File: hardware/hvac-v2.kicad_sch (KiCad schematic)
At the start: 143 parts

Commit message: Start hardware revision 2.3: fix LCD I2C
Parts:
- BZ1: value (none) -> Buzzer; footprint (none) -> Homebrew:MURATA_PKM13EPYH4000-A0
- C1, C14, C38, C9: value (none) -> 4.7uF; footprint (none) -> Capacitor_SMD:C_0603_1608Metric
- C10, C11, C15, C16: value (none) -> 0.22uF; footprint (none) -> Capacitor_SMD:C_0805_2012Metric
- C12, C13, C17, C18, C2, C21, C22, C23, C24, C25, C26, C27, C28, C29, C30, C31, C32, C33, C34, C35, C36, C37, C4, C40, C41, C42, C43, C5, C6, C7, C8: value (none) -> 0.1uF; footprint (none) -> Capacitor_SMD:C_0402_1005Metric
- C19, C39: value (none) -> 1000uF; footprint (none) -> Capacitor_THT:CP_Radial_D10.0mm_P5.00mm
- C20, C3: value (none) -> 1nF; footprint (none) -> Capacitor_SMD:C_0402_1005Metric
- D1, D10, D11, D12, D13, D14, D15, D19, D2, D20, D21, D22, D23, D24, D6, D7: value (none) -> TVS_5V; footprint (none) -> Diode_SMD:D_SOD-323
- D16, D17, D18, D3, D8, D9: value (none) -> D_Schottky; footprint (none) -> Diode_THT:D_DO-201AD_P12.70mm_Horizontal
- D4: value (none) -> TVS_12V; footprint (none) -> Diode_SMD:D_SMB_Handsoldering
- D5: value (none) -> LED; footprint (none) -> LED_SMD:LED_0805_2012Metric
- F1: value (none) -> ATC; footprint (none) -> Homebrew:FUSE_3550-2
- H1, H2, H3, H4, H5: value (none) -> HOLE; footprint (none) -> Homebrew:HOLE_M4
- H6: value (none) -> SLOT; footprint (none) -> Homebrew:SLOT_W2mm_H8mm
- J1: value (none) -> Anderson_two_redblack; footprint (none) -> Homebrew:Anderson_1336G1_right_angle_bottom_two
- J10, J3, J9: value (none) -> Conn_01x02; footprint (none) -> Connector_PinHeader_2.54mm:PinHeader_1x02_P2.54mm_Horizontal
- J11, J12, J13, J5, J6: value (none) -> Conn_01x03; footprint (none) -> Connector_PinHeader_2.54mm:PinHeader_1x03_P2.54mm_Horizontal
- J14, J2: value (none) -> Conn_01x04; footprint (none) -> Connector_PinHeader_2.54mm:PinHeader_1x04_P2.54mm_Horizontal
- J4: value (none) -> Anderson_two_redblack_src; footprint (none) -> Homebrew:Anderson_1336G1_right_angle_bottom_two
- J7, J8: value (none) -> Anderson_two_redblack_sink; footprint (none) -> Homebrew:Anderson_1336G1_right_angle_bottom_two
- JP1, JP2: value (none) -> SolderJumper_2_Open; footprint (none) -> Jumper:SolderJumper-2_P1.3mm_Open_TrianglePad1.0x1.5mm
- Q1, Q2, Q3: value (none) -> AO3400A; footprint (none) -> Package_TO_SOT_SMD:SOT-23
- R1, R14: value (none) -> 470; footprint (none) -> Resistor_SMD:R_0603_1608Metric
- R10, R11, R12, R17, R18, R19, R20, R3, R30, R32, R33, R4, R5: value (none) -> 10k; footprint (none) -> Resistor_SMD:R_0603_1608Metric
- R13, R15, R23, R24, R34, R35, R36, R37, R7: value (none) -> 150; footprint (none) -> Resistor_SMD:R_0603_1608Metric
- R16: value (none) -> 47; footprint (none) -> Resistor_SMD:R_0603_1608Metric
- R2, R21, R22, R6: value (none) -> 24k; footprint (none) -> Resistor_SMD:R_0603_1608Metric
- R25, R26, R27, R28: value (none) -> 4k7; footprint (none) -> Resistor_SMD:R_0603_1608Metric
- R29, R9: value (none) -> 110k; footprint (none) -> Resistor_SMD:R_0603_1608Metric
- R8: value (none) -> 390k; footprint (none) -> Resistor_SMD:R_0603_1608Metric
- SW1: value (none) -> SW_Push; footprint (none) -> Homebrew:SW_TACTILE_5.1MM_TS-1187A-C-D-B
- SW2: value (none) -> Rotary_Encoder_Switch; footprint (none) -> Homebrew:BOURNS_PEC12R-4xxxF-Sxxxx
- U1: value (none) -> STM32F030C8Tx; footprint (none) -> Package_QFP:LQFP-48_7x7mm_P0.5mm
- U2, U3: value (none) -> IFX007T; footprint (none) -> Package_TO_SOT_SMD:TO-263-7_TabPin8
- U4: value (none) -> AMS1117-3.3; footprint (none) -> Package_TO_SOT_SMD:SOT-223-3_TabPin2
- U5: value (none) -> DS18B20; footprint (none) -> Package_TO_SOT_THT:TO-92_Inline
- U6: value (none) -> AMS1117-5.0; footprint (none) -> Package_TO_SOT_SMD:SOT-223-3_TabPin2
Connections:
- net SCL: now also U1.35 (PF6); no longer U1.6 (PF1)
- net SDA: now also U1.36 (PF7); no longer U1.5 (PF0)

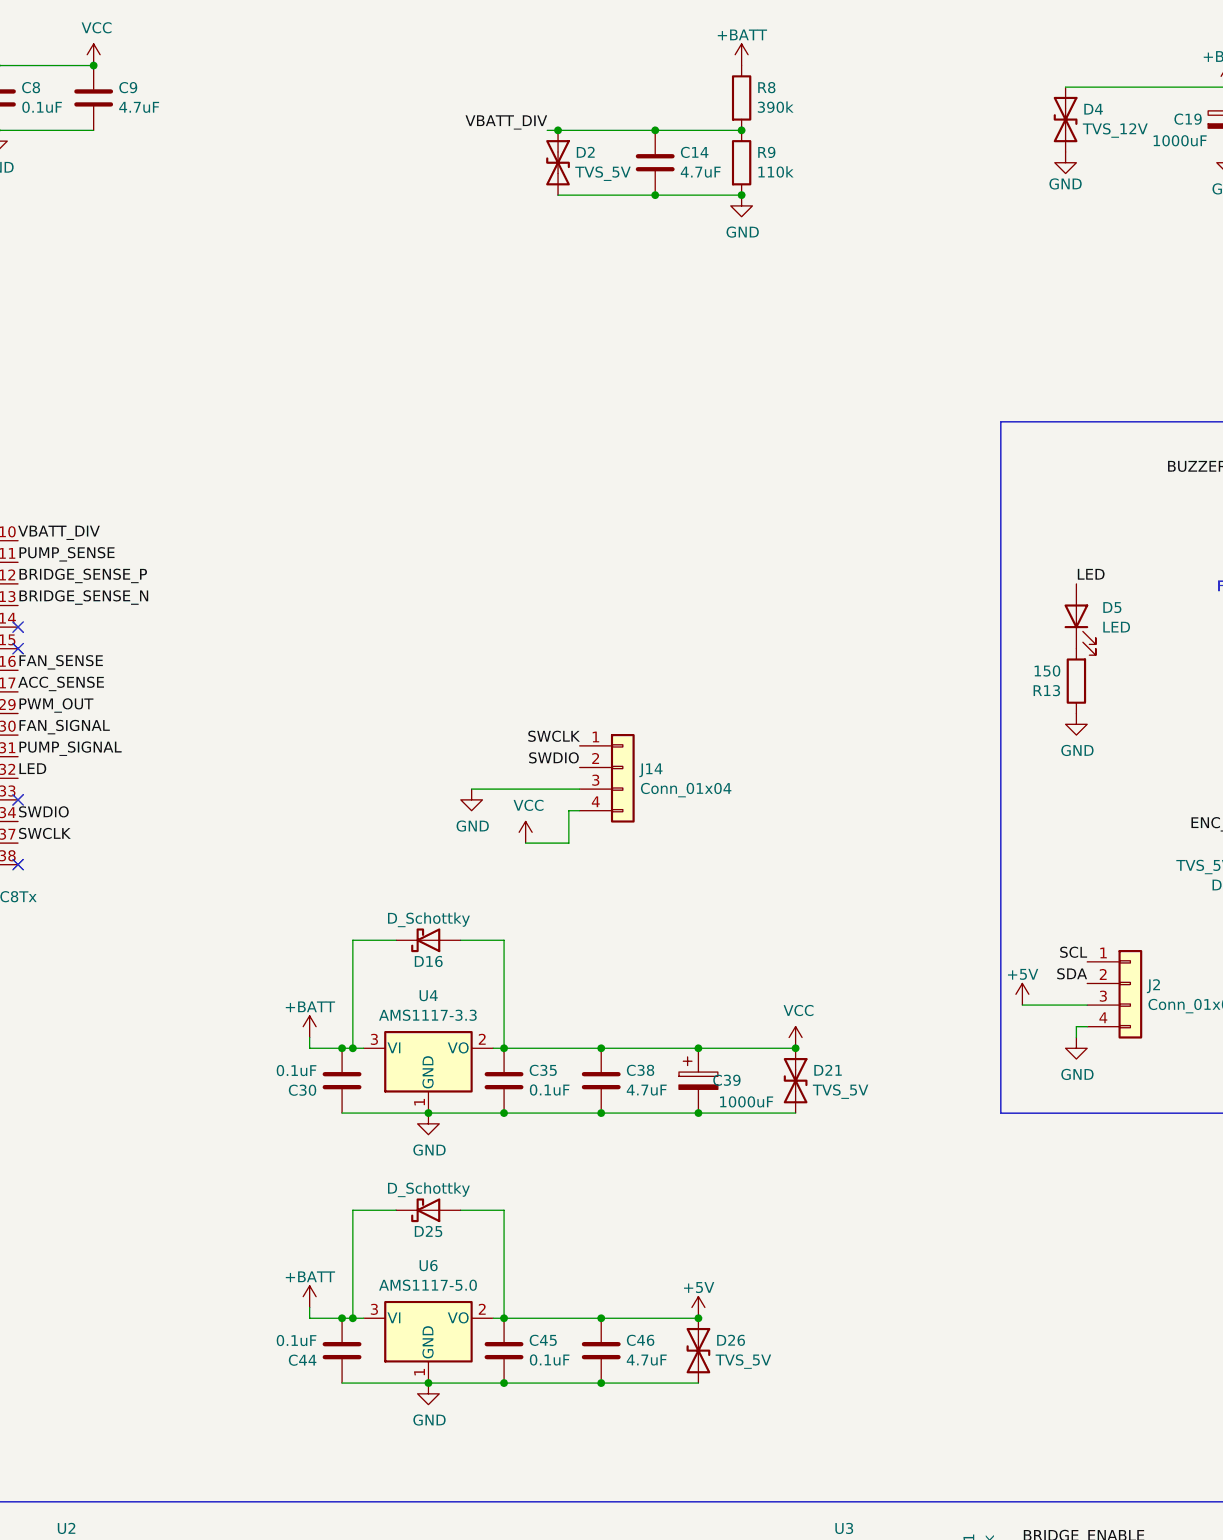
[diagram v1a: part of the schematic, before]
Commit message: Complete hardware v2.3:
- Fix LCD I2C pins
- Switch to voltage regulators with higher input voltage range
- Increase 12v line TVS diodes
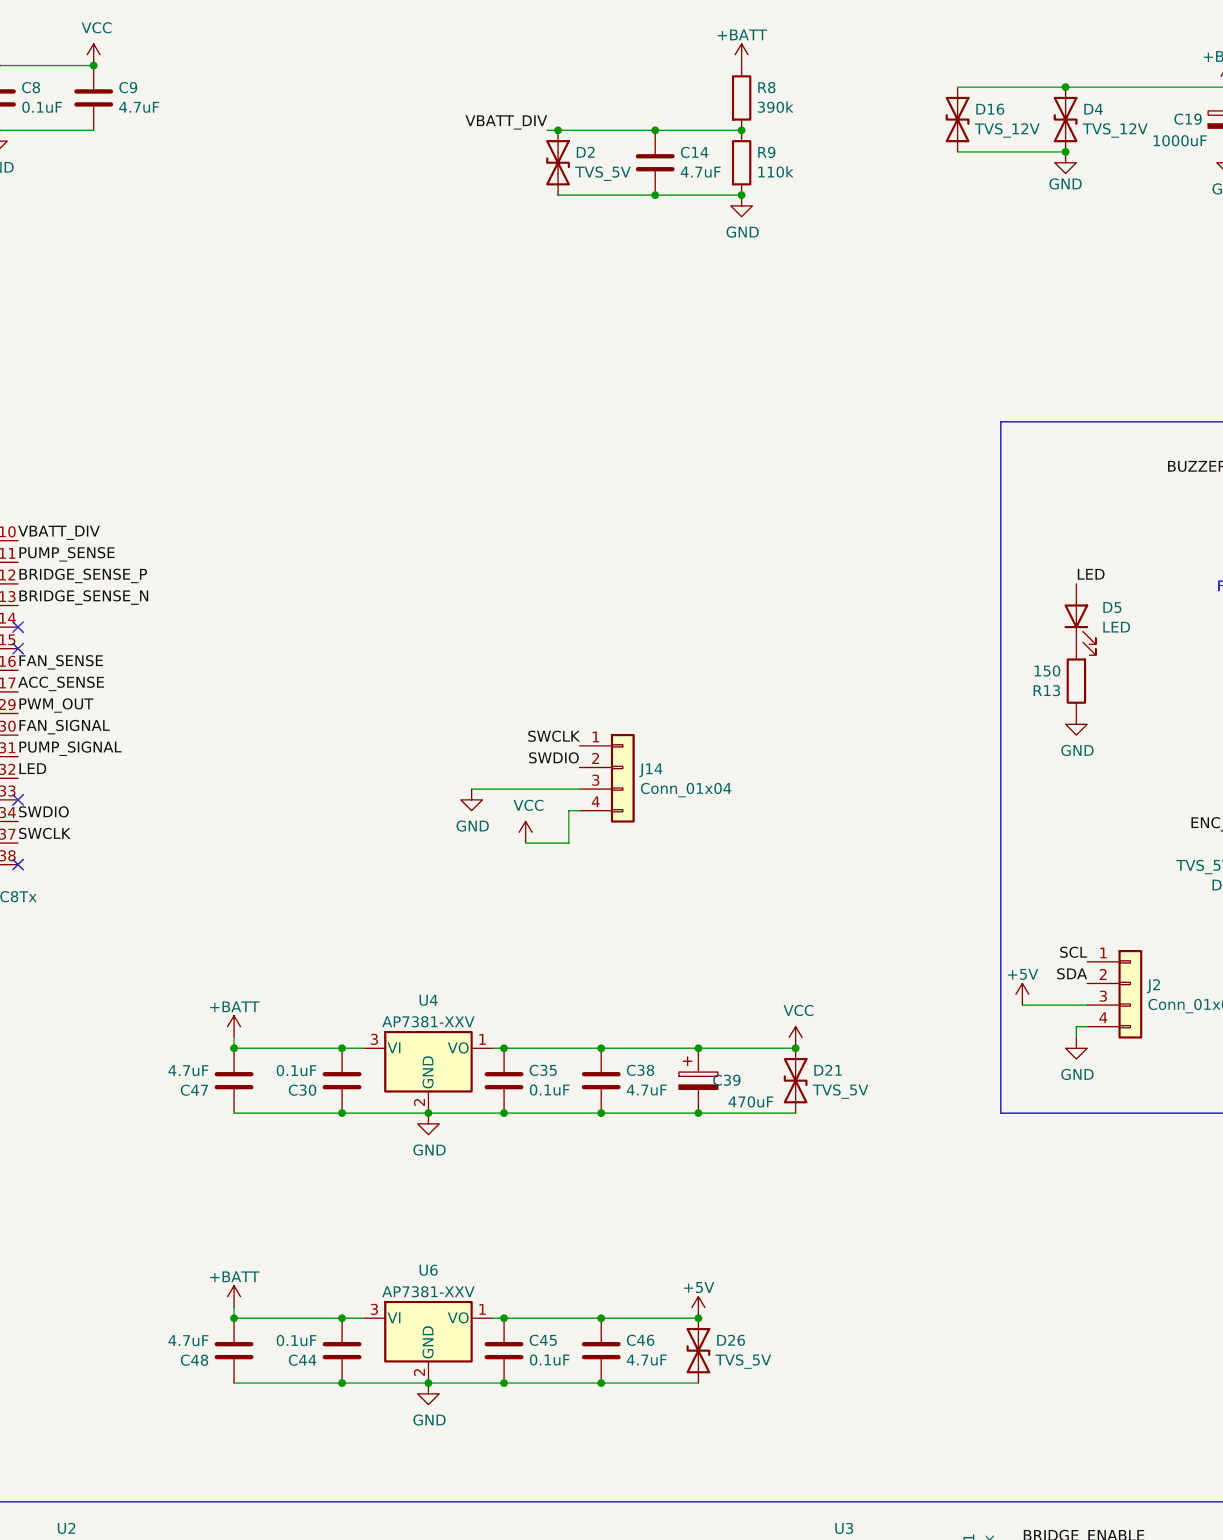
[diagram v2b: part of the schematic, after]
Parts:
- removed D16, D25: D_Schottky, Diode_THT:D_DO-201AD_P12.70mm_Horizontal, symbol Device:D_Schottky
- removed U4: AMS1117-3.3, Package_TO_SOT_SMD:SOT-223-3_TabPin2, symbol Regulator_Linear:AMS1117-3.3
- removed U6: AMS1117-5.0, Package_TO_SOT_SMD:SOT-223-3_TabPin2, symbol Regulator_Linear:AMS1117-5.0
- added C47, C48: 4.7uF, Capacitor_SMD:C_0603_1608Metric, symbol Device:C
- added D16: TVS_12V, Diode_SMD:D_SMB_Handsoldering, symbol Device:D_TVS
- added U4, U6: AP7381-XXV, Package_TO_SOT_THT:TO-92L_Inline_Wide, symbol Homebrew:AP7381-XXV
- C39: value 1000uF -> 470uF
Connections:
- net +5V: now also U6.1 (VO)
- net +BATT: now also C47.2, C48.2, D16.1 (A1), U4.3 (VI), U6.3 (VI)
- net GND: now also C47.1, C48.1, D16.2 (A2), U4.2 (GND), U6.2 (GND)
- net VCC: now also U4.1 (VO)

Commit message: Start updating schematic for v2.4
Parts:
- added D?: TVS_12V, Diode_SMD:D_SMB_Handsoldering, symbol Device:D_TVS
- added Q?: AO3400A, Package_TO_SOT_SMD:SOT-23, symbol Transistor_FET:AO3400A
- added R? (x4): 1k, Resistor_SMD:R_0603_1608Metric, symbol Device:R
- added R? (x5): 150, Resistor_SMD:R_0603_1608Metric, symbol Device:R
- C10, C11, C15, C16: value 0.22uF -> 220nF
- C12, C13, C17, C18, C2, C22, C23, C24, C25, C26, C28, C29, C30, C31, C32, C33, C34, C35, C36, C37, C4, C40, C41, C42, C43, C44, C45, C5, C6, C7, C8: value 0.1uF -> 100nF
- C21, C27: value 0.1uF -> 10nF; LCSC C307331 -> C15195
- R34, R35, R36, R37: value 150 -> 1k
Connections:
- net BRIDGE_SENSE_N: now also R?.1; no longer C20.1, R14.1, U3.6 (IS)
- net BRIDGE_SENSE_P: now also R?.2; no longer C3.1, R1.1, U2.6 (IS)
- net BUTTON: now also U1.14 (PA4), R?.1; no longer C24.1, D10.1 (A1), SW2.S1
- net FAN_SIGNAL: now also R?.1
- net GND: now also D?.2 (A2), Q?.2 (S)
- net TEMP_AUX: now also R?.2; no longer D24.1 (A1), J13.2 (Pin_2), R28.2
- net TEMP_BUILTIN: now also R?.1; no longer R25.2, U5.2 (DQ)
- net TEMP_INSIDE: now also R?.2; no longer D22.1 (A1), J11.2 (Pin_2), R26.2
- net TEMP_OUTSIDE: now also R?.2; no longer D23.1 (A1), J12.2 (Pin_2), R27.2
- net VBATT_DIV: now also R?.1; no longer C14.1, D2.1 (A1), R8.2, R9.1
- net at JP2.1 (A), Q1.3 (D), R6.1: now also D?.1 (A1), Q?.3 (D)
- new net: C14.1, D2.1 (A1), R8.2, R9.1, R?.2
- new net: C3.1, R1.1, R?.1, U2.6 (IS)
- new net: C20.1, R14.1, R?.2, U3.6 (IS)
- new net: R25.2, R?.2, U5.2 (DQ)
- new net: D22.1 (A1), J11.2 (Pin_2), R26.2, R?.1
- new net: D23.1 (A1), J12.2 (Pin_2), R27.2, R?.1
- new net: D24.1 (A1), J13.2 (Pin_2), R28.2, R?.1
- new net: C24.1, D10.1 (A1), R?.2, SW2.S1
- new net: Q?.1 (G), R?.2
- no-connect marks 10 -> 9
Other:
- moved on the sheet: BZ1, C21, C22, C23, C24, C27, C40, D10, D13, D22, D23, D24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

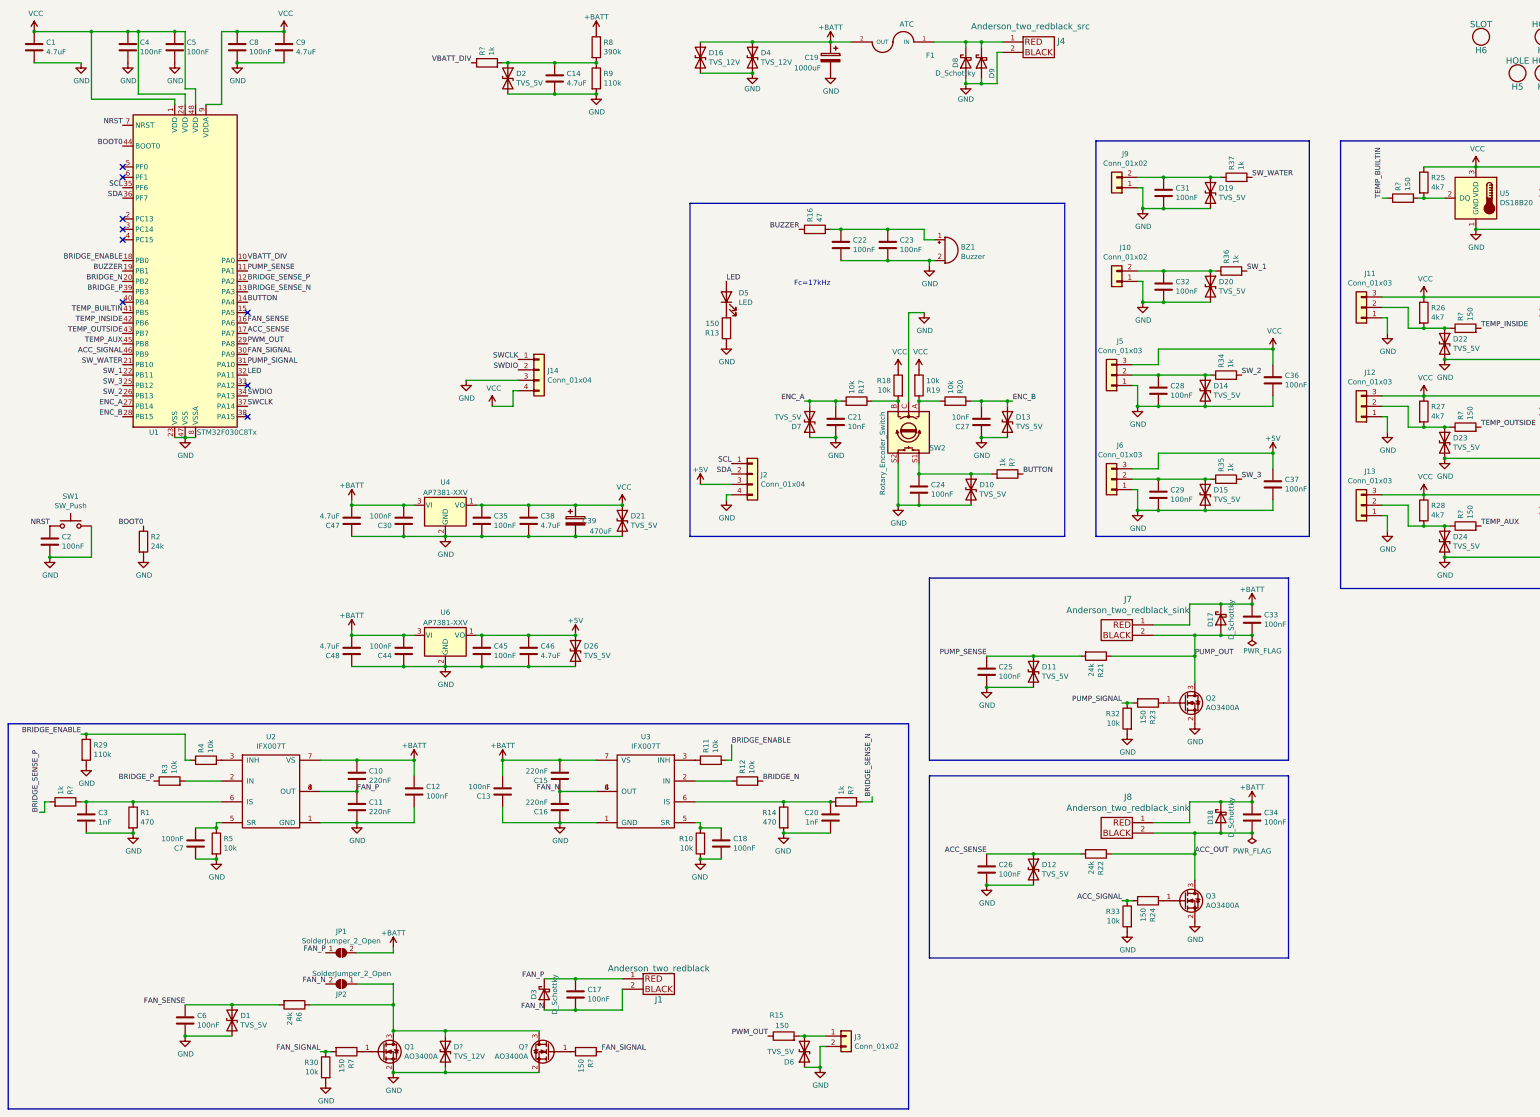
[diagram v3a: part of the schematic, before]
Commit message: Hardware revision 2.4:
- Actually wire encoder button to processor
- Increase power trace widths
- Fix encoder RC circuit cap size
- Add silk labels on top
- Add protection resistors to all IO
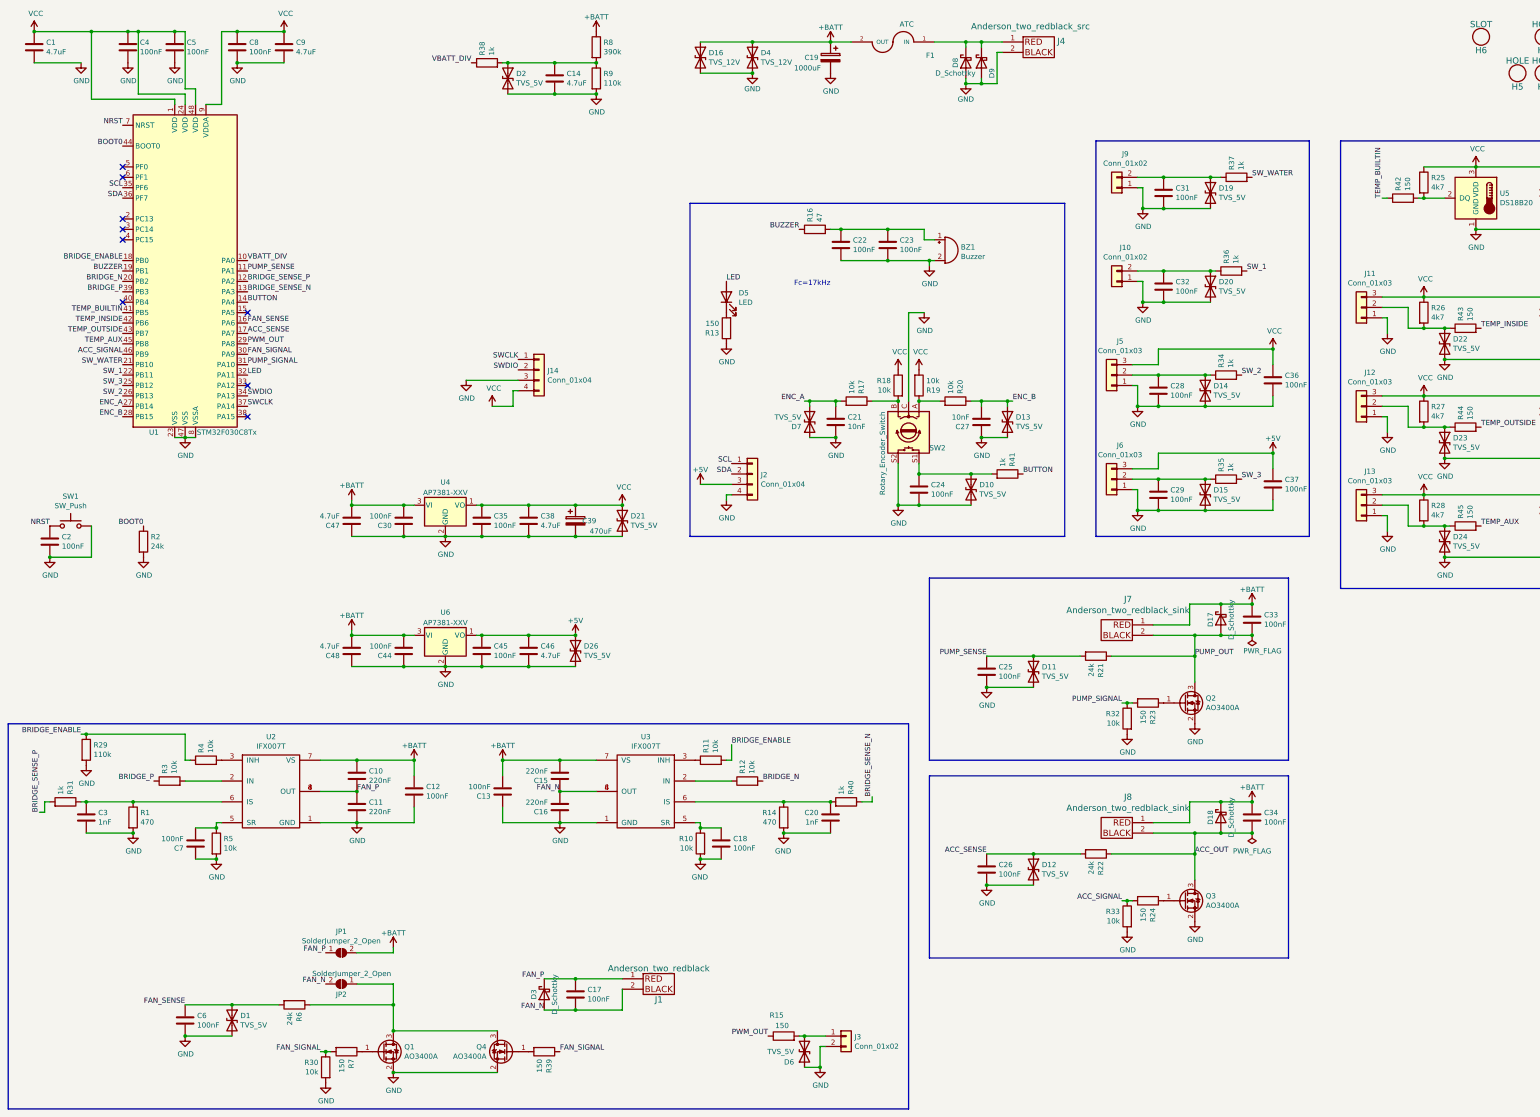
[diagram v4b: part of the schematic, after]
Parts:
- removed D?: TVS_12V, Diode_SMD:D_SMB_Handsoldering, symbol Device:D_TVS
- gave numbers to parts that had none: 10
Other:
- moved on the sheet: Q4, R39
